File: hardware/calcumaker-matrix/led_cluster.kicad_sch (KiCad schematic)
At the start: 64 parts

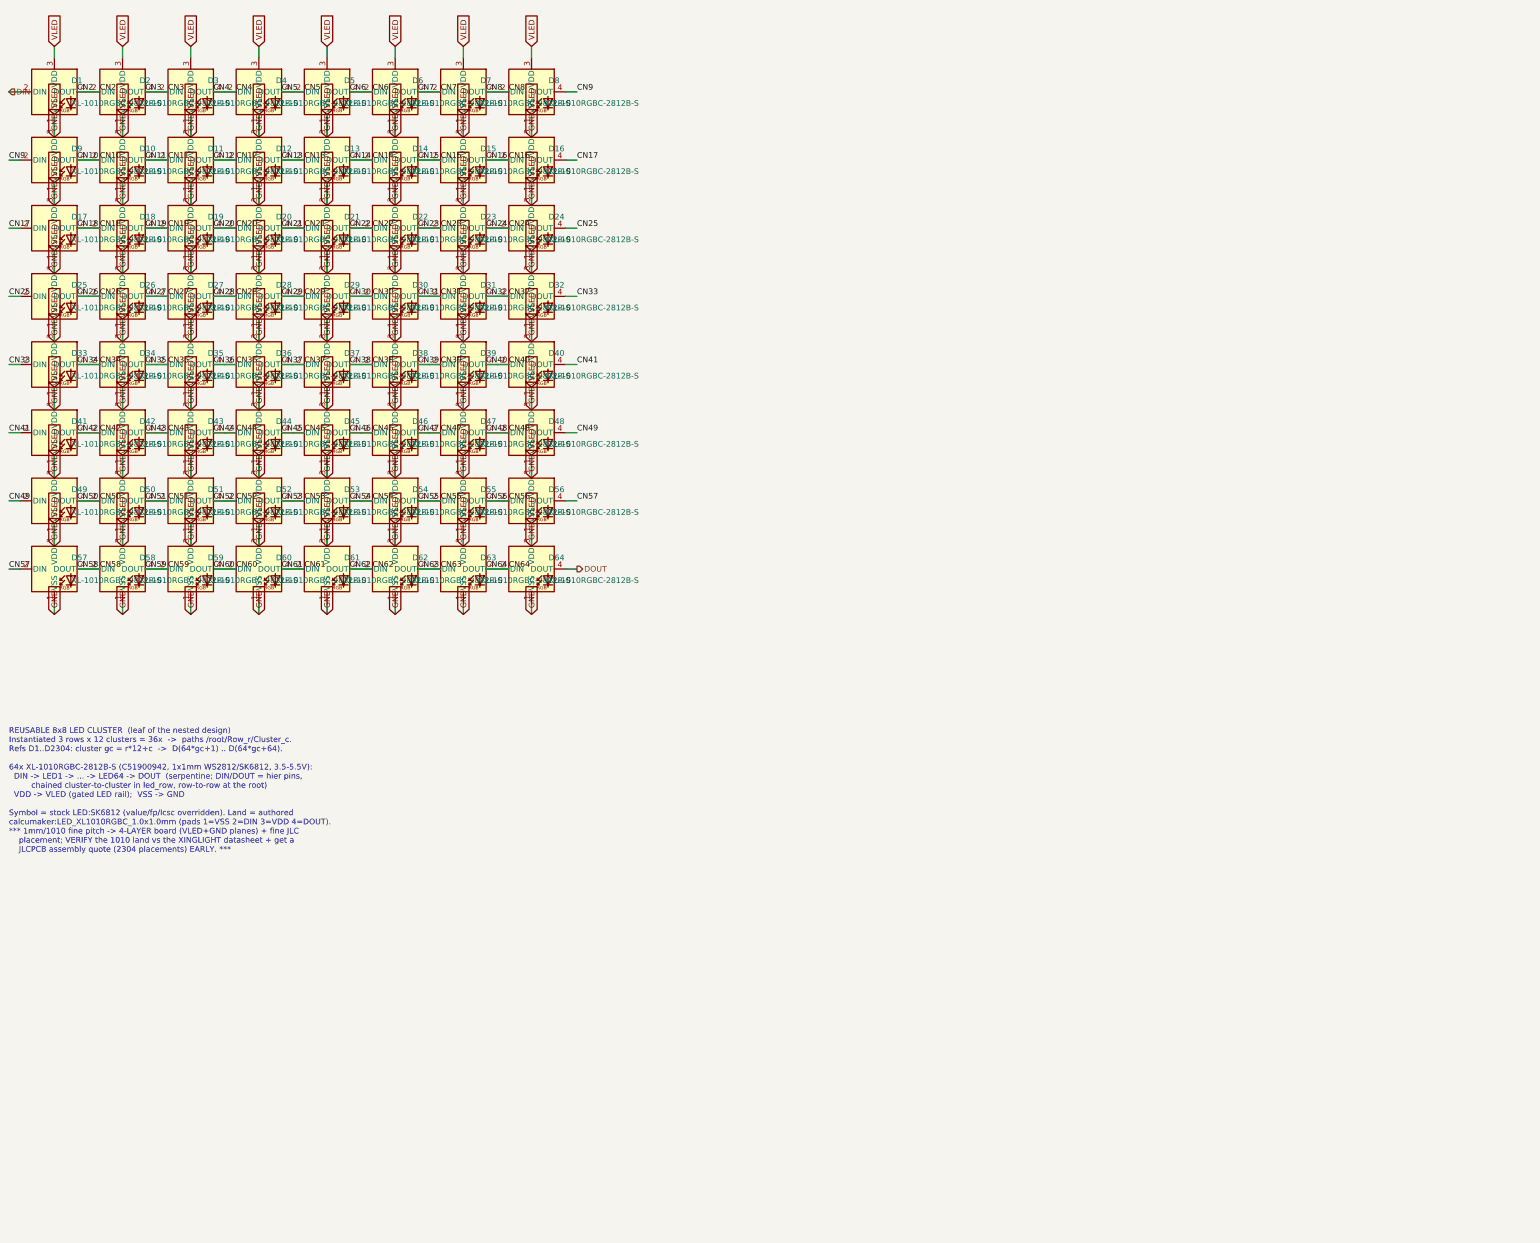
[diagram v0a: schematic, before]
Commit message: Floorplan both display PCBs and verify their schematic nets
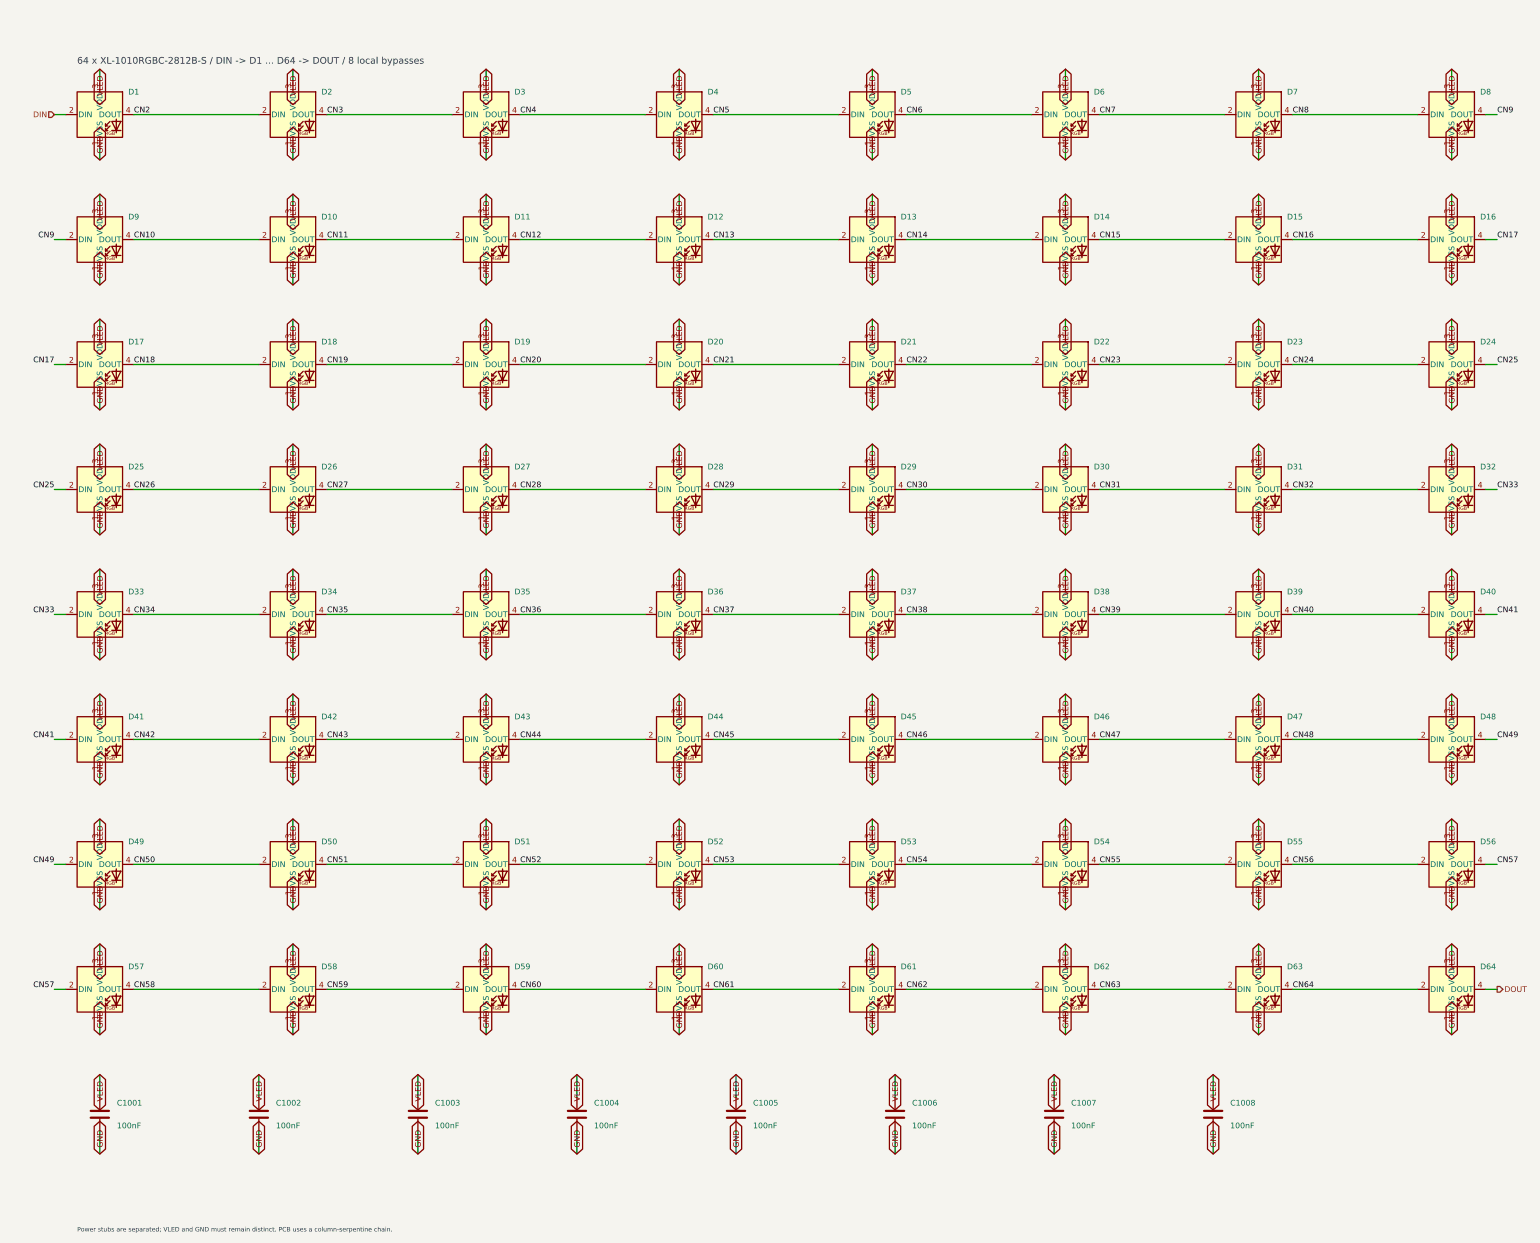
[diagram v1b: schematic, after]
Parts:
- added C1001, C1002, C1003, C1004, C1005, C1006, C1007, C1008: 100nF, Capacitor_SMD:C_0402_1005Metric, symbol Device:C
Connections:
- net GND: now also C1001.2, C1002.2, C1003.2, C1004.2, C1005.2, C1006.2, C1007.2, C1008.2; no longer D1.3 (VDD), D10.3 (VDD), D11.3 (VDD), D12.3 (VDD), D13.3 (VDD), D14.3 (VDD), D15.3 (VDD), D16.3 (VDD), D17.3 (VDD), D18.3 (VDD), D19.3 (VDD), D2.3 (VDD), D20.3 (VDD), D21.3 (VDD), D22.3 (VDD), D23.3 (VDD), D24.3 (VDD), D25.3 (VDD), D26.3 (VDD), D27.3 (VDD), D28.3 (VDD), D29.3 (VDD), D3.3 (VDD), D30.3 (VDD), D31.3 (VDD), D32.3 (VDD), D33.3 (VDD), D34.3 (VDD), D35.3 (VDD), D36.3 (VDD), D37.3 (VDD), D38.3 (VDD), D39.3 (VDD), D4.3 (VDD), D40.3 (VDD), D41.3 (VDD), D42.3 (VDD), D43.3 (VDD), D44.3 (VDD), D45.3 (VDD), D46.3 (VDD), D47.3 (VDD), D48.3 (VDD), D49.3 (VDD), D5.3 (VDD), D50.3 (VDD), D51.3 (VDD), D52.3 (VDD), D53.3 (VDD), D54.3 (VDD), D55.3 (VDD), D56.3 (VDD), D57.3 (VDD), D58.3 (VDD), D59.3 (VDD), D6.3 (VDD), D60.3 (VDD), D61.3 (VDD), D62.3 (VDD), D63.3 (VDD), D64.3 (VDD), D7.3 (VDD), D8.3 (VDD), D9.3 (VDD)
- new net VLED: C1001.1, C1002.1, C1003.1, C1004.1, C1005.1, C1006.1, C1007.1, C1008.1, D1.3 (VDD), D10.3 (VDD), D11.3 (VDD), D12.3 (VDD), D13.3 (VDD), D14.3 (VDD), D15.3 (VDD), D16.3 (VDD), D17.3 (VDD), D18.3 (VDD), D19.3 (VDD), D2.3 (VDD), D20.3 (VDD), D21.3 (VDD), D22.3 (VDD), D23.3 (VDD), D24.3 (VDD), D25.3 (VDD), D26.3 (VDD), D27.3 (VDD), D28.3 (VDD), D29.3 (VDD), D3.3 (VDD), D30.3 (VDD), D31.3 (VDD), D32.3 (VDD), D33.3 (VDD), D34.3 (VDD), D35.3 (VDD), D36.3 (VDD), D37.3 (VDD), D38.3 (VDD), D39.3 (VDD), D4.3 (VDD), D40.3 (VDD), D41.3 (VDD), D42.3 (VDD), D43.3 (VDD), D44.3 (VDD), D45.3 (VDD), D46.3 (VDD), D47.3 (VDD), D48.3 (VDD), D49.3 (VDD), D5.3 (VDD), D50.3 (VDD), D51.3 (VDD), D52.3 (VDD), D53.3 (VDD), D54.3 (VDD), D55.3 (VDD), D56.3 (VDD), D57.3 (VDD), D58.3 (VDD), D59.3 (VDD), D6.3 (VDD), D60.3 (VDD), D61.3 (VDD), D62.3 (VDD), D63.3 (VDD), D64.3 (VDD), D7.3 (VDD), D8.3 (VDD), D9.3 (VDD)
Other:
- note added: "64 x XL-1010RGBC-2812B-S / DIN -> D1 ... D64 -> DOUT / 8 local bypasses"
- note added: "Power stubs are separated; VLED and GND must remain distinct. PCB uses a column-serpentine chain."
- note removed: "REUSABLE 8x8 LED CLUSTER (leaf of the nested design) Instantiated 3 rows x 12 clusters = 36x -> paths /root/Row_r/Cluster_c. Refs D1..D2304: cluster gc = r*12+c -> D(64*gc+1) .. D(64*gc+64). 64x XL-1010RGBC-2812B-S (C51900942, 1x1mm WS2812/SK6812, 3.5-5.5V): DIN -> LED1 -> ... -> LED64 -> DOUT (serpentine; DIN/DOUT = hier pins, chained cluster-to-cluster in led_row, row-to-row at the root) VDD ->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"
- title: Calcumaker 16 — RGB Matrix — Reusable 8x8 RGB cluster (64x XL-1010) -> Calcumaker 16 / matrix / led cluster
- moved on the sheet: D1, D10, D11, D12, D13, D14, D15, D16, D17, D18, D19, D2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
